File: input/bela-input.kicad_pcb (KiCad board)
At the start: 2 copper layers, 114.3 x 35.6 mm, 67 parts, among them P1 MTA-156-4, P2 in_modular, P3 out_bela, U1 TL074, U2 TL074, U3 TL071

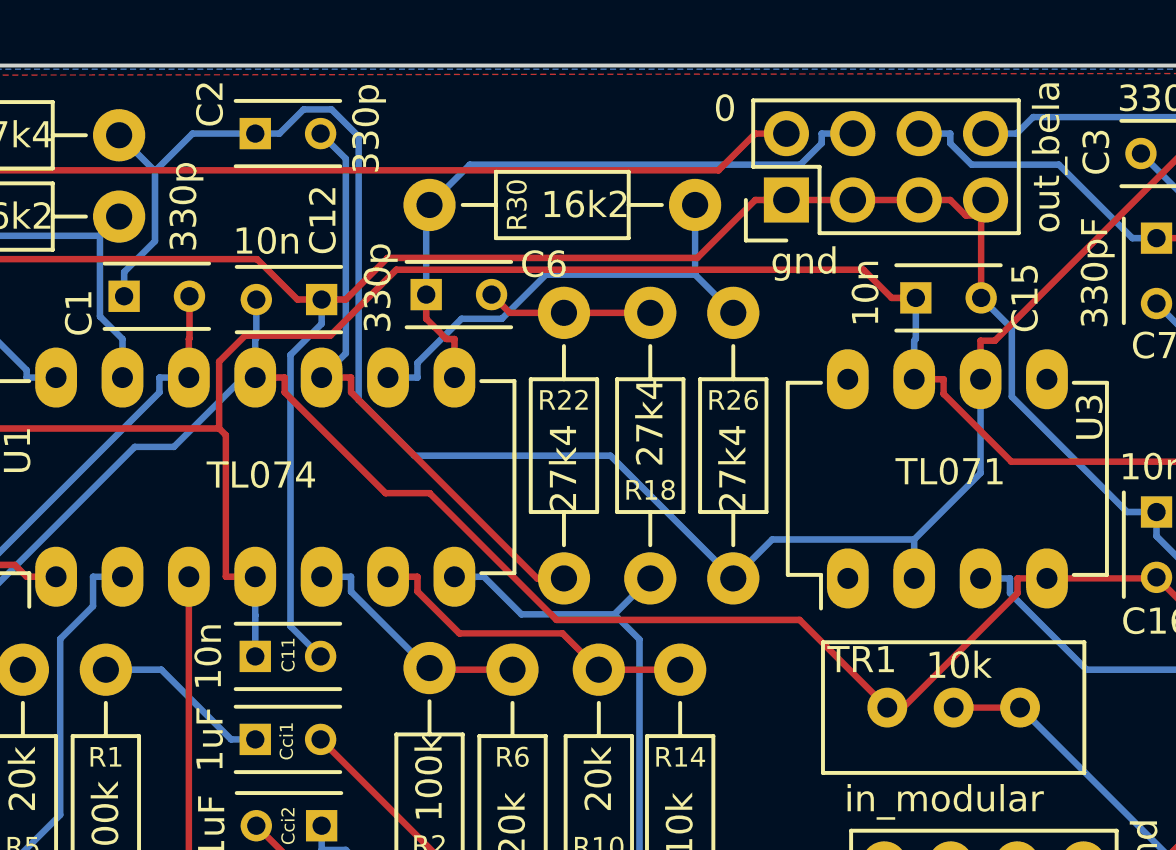
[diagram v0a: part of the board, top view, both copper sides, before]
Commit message: oops, forgot to connect the grounds
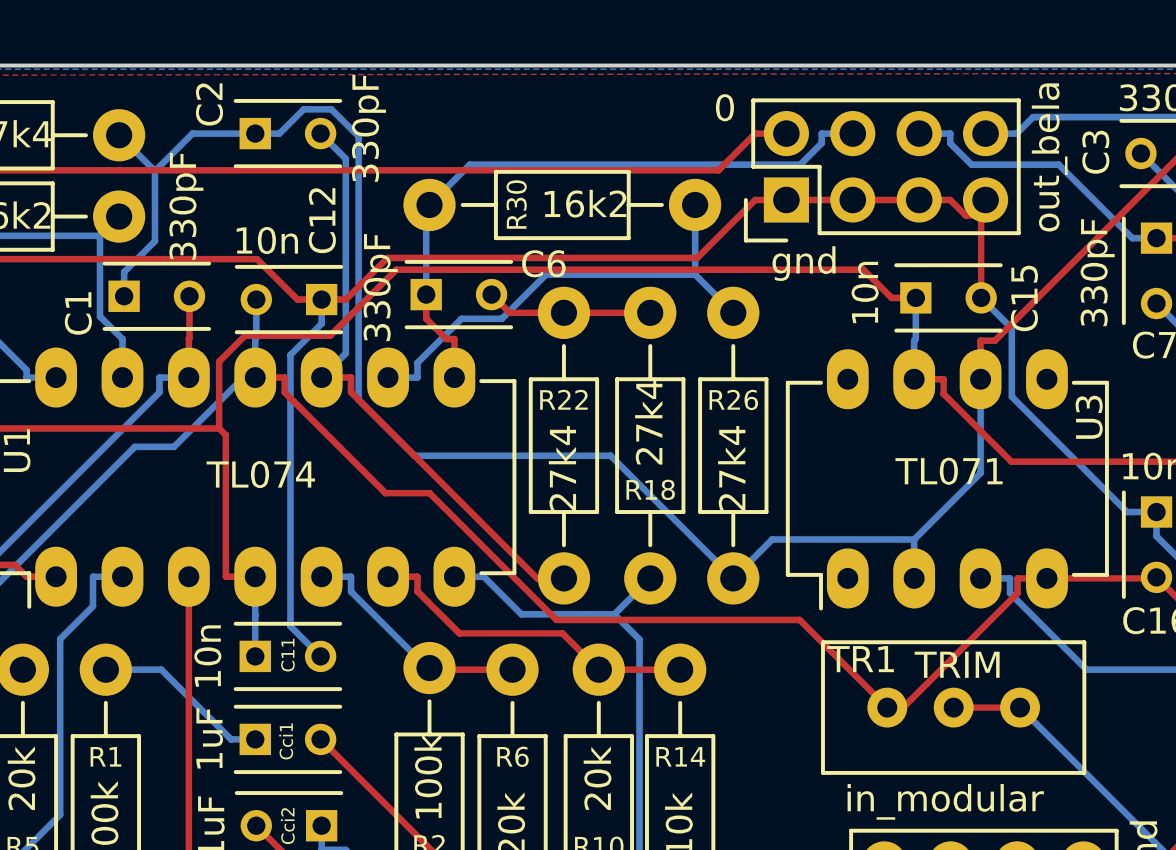
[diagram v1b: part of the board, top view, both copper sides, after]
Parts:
- C1, C2, C6: value 330p -> 330pF
- TR1: value 10k -> TRIM
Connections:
- R10 pad 2: Net-(R10-Pad2) -> GND
- R11 pad 2: Net-(R11-Pad2) -> GND
- R12 pad 2: Net-(R12-Pad2) -> GND
- R5 pad 1: Net-(R5-Pad1) -> GND
- R6 pad 1: Net-(R10-Pad2) -> GND
- R7 pad 1: Net-(R11-Pad2) -> GND
- R8 pad 1: Net-(R12-Pad2) -> GND
- R9 pad 2: Net-(R5-Pad1) -> GND
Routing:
- net GND: track 194.5 -> 207.9 mm
- net Net-(R11-Pad2): track 3.77 -> 0.00 mm
- net Net-(R10-Pad2): track 3.30 -> 0.00 mm
- net Net-(R12-Pad2): track 3.18 -> 0.00 mm
- net Net-(R5-Pad1): track 3.14 -> 0.00 mm
